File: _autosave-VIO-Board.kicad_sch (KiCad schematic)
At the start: 17 parts, among them J1 Conn_01x02_Female, J2 USB_B_Micro, J3 Conn_01x09_Male, J4 Conn_01x09_Male, J5 Conn_01x09_Male, J6 Conn_01x09_Female, J7 Conn_01x09_Female, J8 Conn_01x09_Female

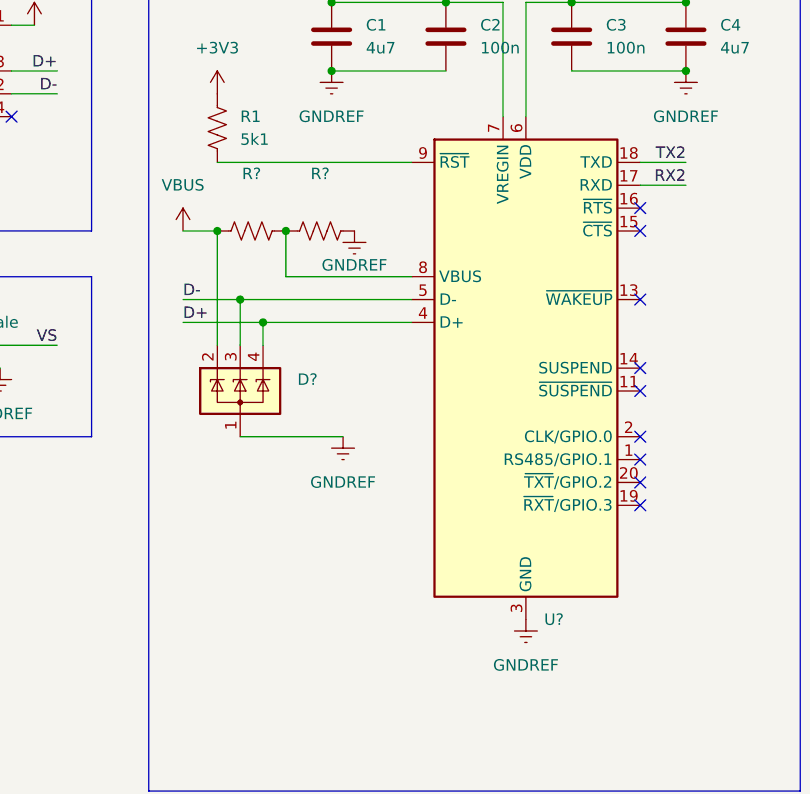
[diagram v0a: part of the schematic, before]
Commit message: new package, ESD protection, fixes
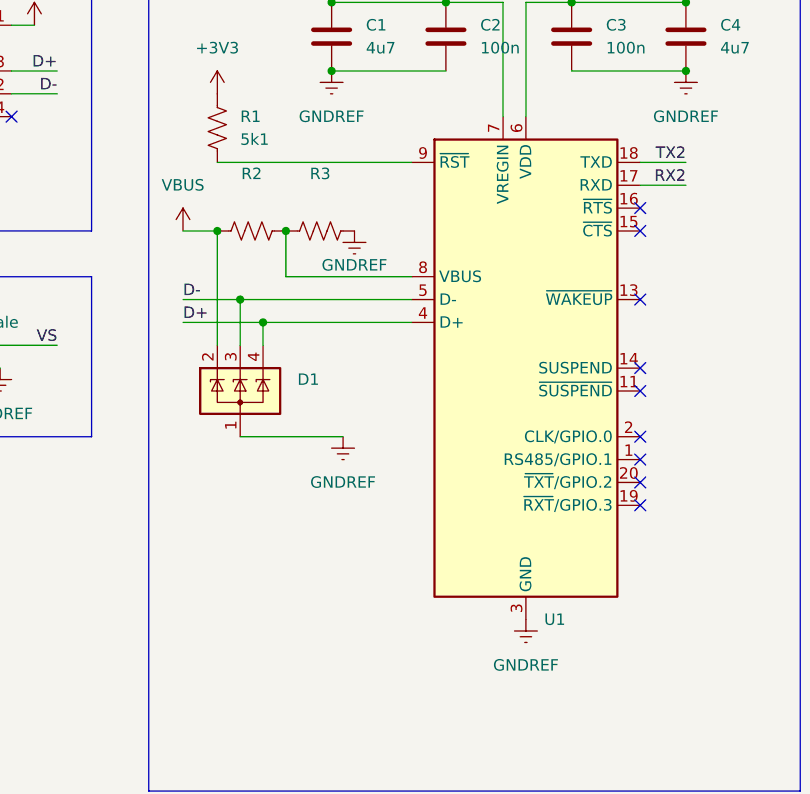
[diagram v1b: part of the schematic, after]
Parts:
- gave numbers to parts that had none: 4
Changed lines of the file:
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@@
   (symbol (lib_id "power:GNDREF") (at 80.01 66.04 0) (unit 1)
     (in_bom yes) (on_board yes)
-    (property "Reference" "#PWR?" (id 0) (at 80.01 72.39 0)
+    (property "Reference" "#PWR09" (id 0) (at 80.01 72.39 0)
       (effects (font (size 1.27 1.27)) hide)
     )
@@
   (symbol (lib_id "Device:R_US") (at 76.2 66.04 90) (unit 1)
     (in_bom yes) (on_board yes) (fields_autoplaced)
-    (property "Reference" "R?" (id 0) (at 76.2 59.69 90))
+    (property "Reference" "R3" (id 0) (at 76.2 59.69 90))
     (property "Value" "" (id 1) (at 76.2 62.23 90))
     (property "Footprint" "" (id 2) (at 76.454 65.024 90)
@@
   (symbol (lib_id "Device:R_US") (at 68.58 66.04 90) (unit 1)
     (in_bom yes) (on_board yes) (fields_autoplaced)
-    (property "Reference" "R?" (id 0) (at 68.58 59.69 90))
+    (property "Reference" "R2" (id 0) (at 68.58 59.69 90))
     (property "Value" "" (id 1) (at 68.58 62.23 90))
     (property "Footprint" "" (id 2) (at 68.834 65.024 90)
@@
   (symbol (lib_id "power:GNDREF") (at 78.74 88.9 0) (unit 1)
     (in_bom yes) (on_board yes) (fields_autoplaced)
-    (property "Reference" "#PWR?" (id 0) (at 78.74 95.25 0)
+    (property "Reference" "#PWR08" (id 0) (at 78.74 95.25 0)
       (effects (font (size 1.27 1.27)) hide)
     )
@@
   (symbol (lib_id "power:+3V3") (at 116.84 40.64 0) (unit 1)
     (in_bom yes) (on_board yes) (fields_autoplaced)
-    (property "Reference" "#PWR09" (id 0) (at 116.84 44.45 0)
+    (property "Reference" "#PWR011" (id 0) (at 116.84 44.45 0)
       (effects (font (size 1.27 1.27)) hide)
     )
@@
   (symbol (lib_id "Interface_USB:CP2102N-Axx-xQFN20") (at 99.06 81.28 0) (unit 1)
     (in_bom yes) (on_board yes) (fields_autoplaced)
-    (property "Reference" "U?" (id 0) (at 101.0794 109.22 0)
+    (property "Reference" "U1" (id 0) (at 101.0794 109.22 0)
       (effects (font (size 1.27 1.27)) (justify left))
     )
@@
   (symbol (lib_id "power:VBUS") (at 77.47 40.64 0) (unit 1)
     (in_bom yes) (on_board yes) (fields_autoplaced)
-    (property "Reference" "#PWR05" (id 0) (at 77.47 44.45 0)
+    (property "Reference" "#PWR06" (id 0) (at 77.47 44.45 0)
       (effects (font (size 1.27 1.27)) hide)
     )
@@
   (symbol (lib_id "power:GNDREF") (at 99.06 109.22 0) (unit 1)
     (in_bom yes) (on_board yes) (fields_autoplaced)
-    (property "Reference" "#PWR08" (id 0) (at 99.06 115.57 0)
+    (property "Reference" "#PWR010" (id 0) (at 99.06 115.57 0)
       (effects (font (size 1.27 1.27)) hide)
     )
@@
   (symbol (lib_id "power:GNDREF") (at 116.84 48.26 0) (unit 1)
     (in_bom yes) (on_board yes) (fields_autoplaced)
-    (property "Reference" "#PWR010" (id 0) (at 116.84 54.61 0)
+    (property "Reference" "#PWR012" (id 0) (at 116.84 54.61 0)
       (effects (font (size 1.27 1.27)) hide)
     )
@@
   (symbol (lib_id "power:GNDREF") (at 77.47 48.26 0) (unit 1)
     (in_bom yes) (on_board yes) (fields_autoplaced)
-    (property "Reference" "#PWR06" (id 0) (at 77.47 54.61 0)
+    (property "Reference" "#PWR07" (id 0) (at 77.47 54.61 0)
       (effects (font (size 1.27 1.27)) hide)
     )
@@
   (symbol (lib_id "power:VBUS") (at 60.96 66.04 0) (unit 1)
     (in_bom yes) (on_board yes) (fields_autoplaced)
-    (property "Reference" "#PWR07" (id 0) (at 60.96 69.85 0)
+    (property "Reference" "#PWR04" (id 0) (at 60.96 69.85 0)
       (effects (font (size 1.27 1.27)) hide)
     )
@@
   (symbol (lib_id "power:+3V3") (at 64.77 50.8 0) (unit 1)
     (in_bom yes) (on_board yes) (fields_autoplaced)
-    (property "Reference" "#PWR04" (id 0) (at 64.77 54.61 0)
+    (property "Reference" "#PWR05" (id 0) (at 64.77 54.61 0)
       (effects (font (size 1.27 1.27)) hide)
     )
@@
   (symbol (lib_id "Power_Protection:SP0503BAHT") (at 67.31 83.82 0) (unit 1)
     (in_bom yes) (on_board yes)
-    (property "Reference" "D?" (id 0) (at 73.66 82.55 0)
+    (property "Reference" "D1" (id 0) (at 73.66 82.55 0)
       (effects (font (size 1.27 1.27)) (justify left))
     )
@@
       (reference "#PWR03") (unit 1) (value "VBUS") (footprint "")
     )
+    (path "/d9d6439f-9b67-4965-963f-2ec0d20a1f84"
+      (reference "#PWR04") (unit 1) (value "VBUS") (footprint "")
+    )
     (path "/e8fd0535-6a40-4369-b4e1-2f7332303594"
-      (reference "#PWR04") (unit 1) (value "+3V3") (footprint "")
+      (reference "#PWR05") (unit 1) (value "+3V3") (footprint "")
     )
     (path "/aaf6d173-f17c-46f4-85ef-8a56f1d078fc"
-      (reference "#PWR05") (unit 1) (value "VBUS") (footprint "")
+      (reference "#PWR06") (unit 1) (value "VBUS") (footprint "")
     )
     (path "/ccbecf91-8464-4655-a9f1-1e717fd2d32f"
-      (reference "#PWR06") (unit 1) (value "GNDREF") (footprint "")
-    )
-    (path "/d9d6439f-9b67-4965-963f-2ec0d20a1f84"
-      (reference "#PWR07") (unit 1) (value "VBUS") (footprint "")
+      (reference "#PWR07") (unit 1) (value "GNDREF") (footprint "")
+    )
+    (path "/56e1cf0e-d61b-4dfe-8d76-cf4629de505d"
+      (reference "#PWR08") (unit 1) (value "GNDREF") (footprint "")
+    )
+    (path "/1085a35a-4fad-41d9-9ca7-e49a6bbaf11c"
+      (reference "#PWR09") (unit 1) (value "GNDREF") (footprint "")
     )
     (path "/bfc19f53-0a87-4bd5-bc60-b8db527a9d57"
-      (reference "#PWR08") (unit 1) (value "GNDREF") (footprint "")
+      (reference "#PWR010") (unit 1) (value "GNDREF") (footprint "")
     )
     (path "/6632dfaa-9ffe-4983-8f63-a437db3aa83c"
-      (reference "#PWR09") (unit 1) (value "+3V3") (footprint "")
+      (reference "#PWR011") (unit 1) (value "+3V3") (footprint "")
     )
     (path "/c088b075-78e4-4c54-8067-d972c3672dc3"
-      (reference "#PWR010") (unit 1) (value "GNDREF") (footprint "")
-    )
-    (path "/1085a35a-4fad-41d9-9ca7-e49a6bbaf11c"
-      (reference "#PWR?") (unit 1) (value "GNDREF") (footprint "")
-    )
-    (path "/56e1cf0e-d61b-4dfe-8d76-cf4629de505d"
-      (reference "#PWR?") (unit 1) (value "GNDREF") (footprint "")
+      (reference "#PWR012") (unit 1) (value "GNDREF") (footprint "")
     )
     (path "/f7a02a4d-5b2a-4743-beba-bffcf39ae8d4"
@@
     )
     (path "/fcb23687-79e7-494b-b78d-610b9b788477"
-      (reference "D?") (unit 1) (value "SP0503BAHT") (footprint "Package_TO_SOT_SMD:SOT-143")
+      (reference "D1") (unit 1) (value "SP0503BAHT") (footprint "Package_TO_SOT_SMD:SOT-143")
     )
     (path "/38b69a3f-9f2a-4119-861c-51e9020433d6"
@@
       (reference "R1") (unit 1) (value "5k1") (footprint "Resistor_SMD:R_0402_1005Metric")
     )
+    (path "/2ff395ea-5491-46d8-9fe0-ef3e45cdd157"
+      (reference "R2") (unit 1) (value "22k1") (footprint "Resistor_SMD:R_0402_1005Metric")
+    )
     (path "/2773960a-b220-4367-b86f-1f2693b6238b"
-      (reference "R?") (unit 1) (value "47k5") (footprint "Resistor_SMD:R_0402_1005Metric")
-    )
-    (path "/2ff395ea-5491-46d8-9fe0-ef3e45cdd157"
-      (reference "R?") (unit 1) (value "22k1") (footprint "Resistor_SMD:R_0402_1005Metric")
+      (reference "R3") (unit 1) (value "47k5") (footprint "Resistor_SMD:R_0402_1005Metric")
     )
     (path "/8c087470-e370-4fb0-9ba5-a82293a7d292"
-      (reference "U?") (unit 1) (value "CP2102N-Axx-xQFN20") (footprint "Package_DFN_QFN:SiliconLabs_QFN-20-1EP_3x3mm_P0.5mm")
-    )
-  )
+      (reference "U1") (unit 1) (value "CP2102N-Axx-xQFN20") (footprint "Package_DFN_QFN:SiliconLabs_QFN-20-1EP_3x3mm_P0.5mm_EP1.8x1.8mm")
+    )
+  )
